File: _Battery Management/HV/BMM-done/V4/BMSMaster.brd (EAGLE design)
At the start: 88.9 x 79.7 mm, 120 parts, among them J1 M2_DF13-2P, J10 IMD, J2 M2_DF13-2P, J3 M4_1X4_LOCK, J4 M80022232081-2, J5 M16_M_194280016, J6 M2770166, J7 M2770166, J8 M2770166, J9 M2770166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

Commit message: BMM cleanup
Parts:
- added RE, RX, TX: TP, FSAE Electric:0603
- moved R6 3.30 mm to (70.5, 50.0), flipped to the bottom
- moved R9 2.80 mm to (68.0, 50.0), flipped to the bottom
- moved K1 2.29 mm to (8.64, 20.1)
- moved U23 2.04 mm to (6.76, 15.2)
- moved J9 1.65 mm to (20.2, 42.7)
- moved J7 0.89 mm to (27.1, 42.7)
- moved J10 0.76 mm to (26.3, 30.9)
- moved J8 0.64 mm to (40.8, 42.7)
- moved U$1 0.63 mm to (47.1, 46.3)
- moved R34 0.38 mm to (37.0, 32.4)
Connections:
- net RE: now also RE.1, RE.2
- net RX2: now also RX.1, RX.2
- net TX2: now also TX.1, TX.2
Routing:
- net VSS: track 103.3 -> 111.7 mm
- net +3V3: track 279.5 -> 271.7 mm, vias 68 -> 67
- net CS2: track 30.3 -> 34.9 mm
- net RX2: track 17.6 -> 22.0 mm
- net RE: track 30.0 -> 34.3 mm
- net TX2: track 21.0 -> 25.0 mm
- net +24V: track 117.0 -> 120.9 mm
- net N$22: track 6.49 -> 3.30 mm, vias 2 -> 1
- net N$3: track 6.37 -> 3.26 mm, vias 2 -> 1
- net BMS-SS: track 57.7 -> 59.8 mm
- net BMS-SET: track 65.9 -> 67.8 mm
- net PRE_CRG-B_AIR: track 23.1 -> 24.0 mm
- net INTERLOCK_IN: track 26.7 -> 26.0 mm
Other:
- outline, holes or cut-outs redrawn

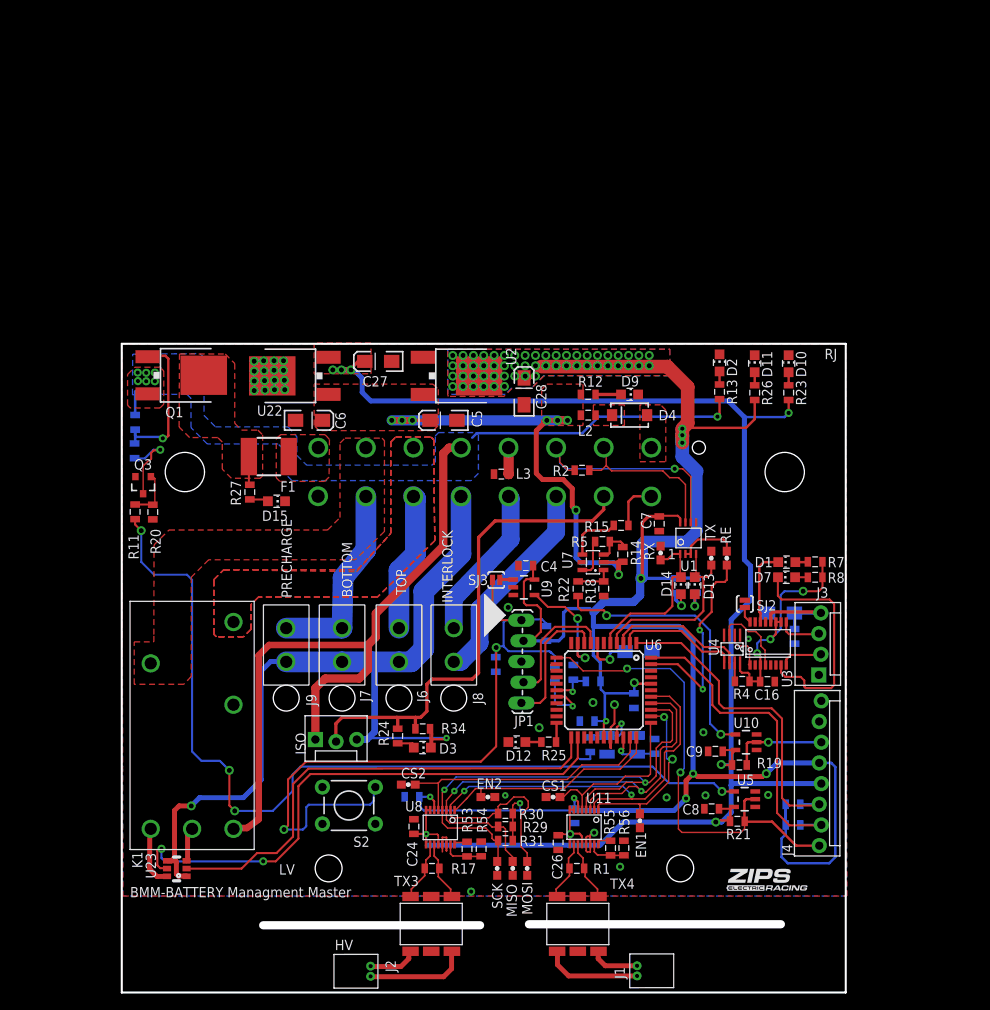
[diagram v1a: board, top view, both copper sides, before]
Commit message: Making board size change, make IO more accessible.
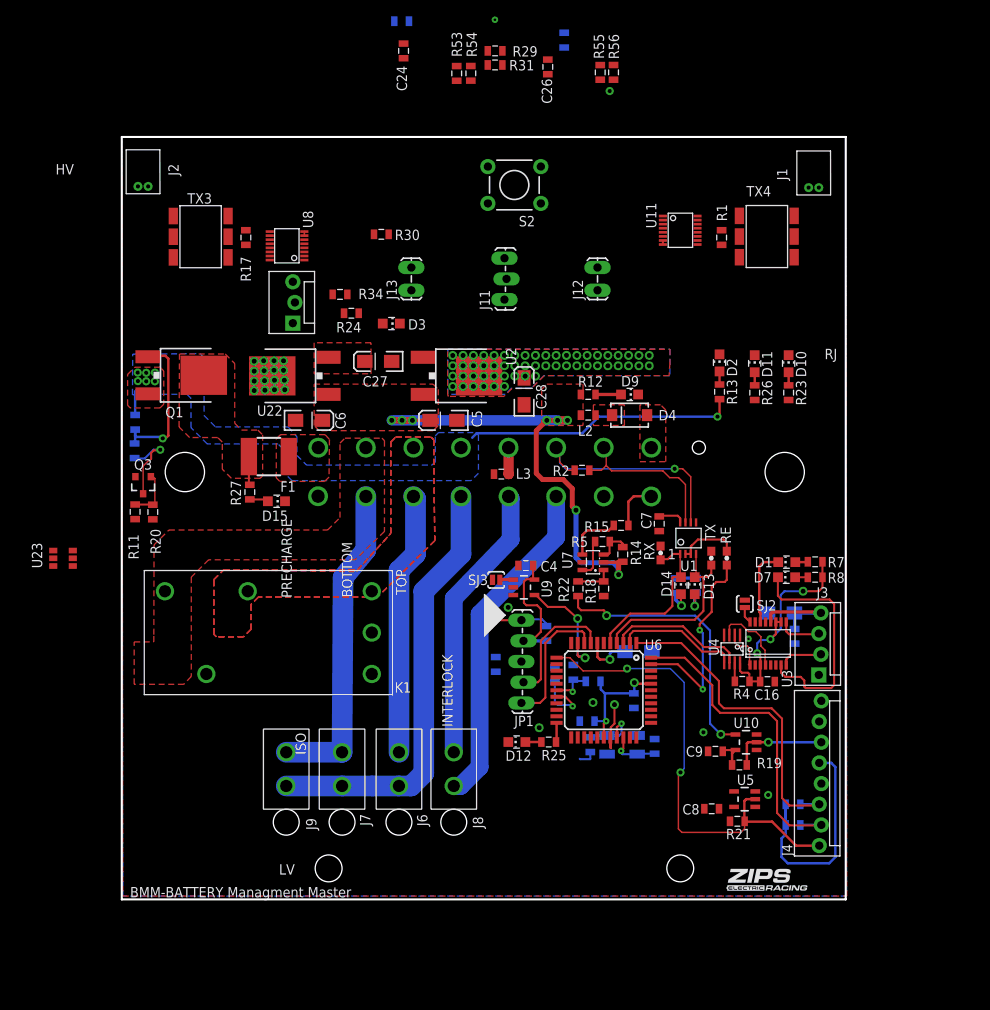
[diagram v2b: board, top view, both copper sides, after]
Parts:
- removed CS1, CS2, EN1, EN2, MISO, MOSI, SCK: TP, FSAE Electric:0603
- added J11: (no value), SparkFun-Connectors:1X03_LOCK_LONGPADS
- added J12, J13: (no value), SparkFun-Connectors:1X02_LOCK_LONGPADS
- moved J2 100.3 mm to (2.61, 99.0), turned to 0 degrees
- moved J1 98.6 mm to (85.0, 98.8), turned to 0 degrees
- moved C23 95.3 mm to (34.4, 119.3)
- moved C24 95.3 mm to (34.6, 115.6)
- moved C25 95.3 mm to (54.3, 117.0)
- moved C26 95.3 mm to (52.3, 113.7)
- moved R29 95.3 mm to (45.8, 115.6)
- moved R31 95.3 mm to (45.8, 113.9)
- moved R53 95.3 mm to (41.1, 112.9)
- moved R54 95.3 mm to (42.9, 112.9)
- moved R55 95.3 mm to (58.8, 113.0)
- moved R56 95.3 mm to (60.4, 113.0)
- moved TX3 89.0 mm to (9.68, 92.8), turned to 180 degrees
- moved TX4 87.6 mm to (79.2, 92.8), turned to 0 degrees
- moved R17 80.8 mm to (15.2, 92.7), turned to 90 degrees
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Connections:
- net CS1: now also J12.2; no longer CS1.1, CS1.2
- net CS2: now also J13.1; no longer CS2.1, CS2.2
- net EN1: now also J12.1; no longer EN1.1, EN1.2
- net EN2: now also J13.2; no longer EN2.1, EN2.2
- net MISO: now also J11.2; no longer MISO.1, MISO.2
- net MOSI: now also J11.3; no longer MOSI.1, MOSI.2
- net SCK: now also J11.1; no longer SCK.1, SCK.2
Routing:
- net +3V3: track 271.7 -> 67.8 mm, vias 67 -> 57
- net +5V: track 203.2 -> 4.64 mm, vias 8 -> 0
- net N$19: track 110.6 -> 0.00 mm, vias 4 -> 0
- net +24V: track 120.9 -> 36.8 mm
- net N$45: track 89.8 -> 6.32 mm, vias 2 -> 0
- net MOSI: track 71.7 -> 0.00 mm, vias 2 -> 0
- net BMS-SET: track 67.8 -> 0.00 mm, vias 2 -> 0
- net MISO: track 67.0 -> 0.00 mm, vias 2 -> 0
- net SCK: track 65.8 -> 0.00 mm, vias 2 -> 0
- net IMD: track 62.1 -> 0.00 mm
- net BMS-SS: track 59.8 -> 0.00 mm
- net VSS: track 111.7 -> 55.5 mm, vias 2 -> 0
- net CS2: track 34.9 -> 0.00 mm
- net EN2: track 30.0 -> 0.00 mm
- net EN1: track 23.9 -> 0.00 mm, vias 2 -> 0
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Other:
- board size 88.9 x 79.7 mm -> 88.9 x 93.6 mm

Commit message: playing w/ layout
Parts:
- moved R23 44.2 mm to (45.7, 99.1)
- moved D10 43.3 mm to (47.0, 102.9), turned to 270 degrees
- moved R26 37.0 mm to (50.8, 99.1)
- moved D11 36.3 mm to (52.1, 102.9), turned to 270 degrees
- moved R13 30.8 mm to (55.9, 99.1)
- moved D2 30.3 mm to (57.1, 102.9), turned to 270 degrees
- moved K1 28.4 mm to (2.32, 46.0), turned to 0 degrees
- moved S2 23.6 mm to (67.3, 85.2)
- moved J9 5.08 mm to (15.1, 27.4)
- moved J7 2.54 mm to (24.5, 27.4)
- moved U11 1.27 mm to (67.3, 93.6)
- moved J6 1.27 mm to (32.8, 27.4)
- moved R1 1.27 mm to (72.4, 92.7)
- moved TX4 1.27 mm to (78.0, 92.8)
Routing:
- net +24V: track 36.8 -> 3.34 mm, vias 7 -> 6
- net VSS: track 55.5 -> 67.7 mm
- net PRE_CRG-B_AIR: track 39.3 -> 42.8 mm
- net N$30: track 2.14 -> 0.00 mm
- net N$9: track 1.90 -> 0.00 mm
- net N$13: track 1.61 -> 0.00 mm
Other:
- board size 88.9 x 93.6 mm -> 88.9 x 94 mm

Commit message: Working on BMM
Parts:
- removed J4: M80022232081-2, FSAE Electric:MOLEX-1X8-2
- removed L5: L_FB_2A, FSAE Electric:0805
- removed STANDOFF3, STANDOFF4: STAND-OFF, SparkFun-Electromechanical:STAND-OFF
- removed U$2: LOGO16-2-M, Pic:2016-2-LOGO-M
- added C10: 0.1UF, FSAE Electric:0805
- added J14: USB_B_RA, FSAE Electric:USB-B1HSW6
- added U12: FT24C64A, FSAE Electric:SOT23-5
- J3: value M4_1X4_LOCK -> M8S08B-PASK-2(LF)(SN); device FSAE Electric:MOLEX_1X4 -> FSAE Electric:S08B-PASK-2(LF)(SN)
- S2: value (none) -> SWITCH-MOMENTARY-2SIDE_EZ; device SparkFun-Electromechanical:TACTILE-PTH -> SparkFun-Electromechanical:TACTILE-PTH-SIDEEZ
- moved D12 74.9 mm to (24.0, 101.5), turned to 0 degrees
- moved R25 72.1 mm to (25.8, 97.8), turned to 90 degrees
- moved C26 70.3 mm to (-11.6, 84.2)
- moved R7 69.3 mm to (34.4, 100.1), flipped to the bottom, turned to 270 degrees
- moved R8 69.1 mm to (36.5, 100.1), flipped to the bottom, turned to 270 degrees
- moved D1 67.2 mm to (34.2, 100.4), turned to 180 degrees
- moved D7 66.9 mm to (36.5, 100.4), turned to 180 degrees
- moved C20 64.6 mm to (41.5, 93.6), turned to 0 degrees
- moved C14 63.8 mm to (40.7, 96.1)
- moved C16 59.3 mm to (52.3, 91.0), flipped to the bottom, turned to 90 degrees
- moved C23 59.1 mm to (65.5, 69.0), turned to 270 degrees
- moved U22 58.3 mm to (76.5, 57.1), turned to 0 degrees
- moved U3 57.7 mm to (47.4, 90.9), turned to 90 degrees
- moved C6 55.6 mm to (74.5, 49.4)
- moved R4 54.7 mm to (51.3, 86.9), flipped to the bottom, turned to 90 degrees
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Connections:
- removed net N$21: C1.1, L5.2, U6.17
- net +3V3: now also C1.1, C10.1, J3.3, U12.4, U6.17; no longer J4.5, L5.1
- net +5V: now also J3.6; no longer J4.4
- net CS: now also J3.1; no longer J4.6
- net GND: now also C10.2, J14.4, J3.7, J3.8, U12.2, U12.5; no longer J3.1, J4.7, J4.8
- net HV-SENSE: now also J3.2; no longer J4.1
- net N$16: now also J14.2; no longer J3.3
- net N$18: now also J14.3; no longer J3.2
- net N$45: now also S2.2; no longer S2.3
- net N$85: now also J14.1; no longer J3.4
- net SCL: now also J3.5, U12.1; no longer J4.2
- net SDA: now also J3.4, U12.3; no longer J4.3
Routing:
- net MOSI: track 0.00 -> 97.4 mm, vias 0 -> 2
- net MISO: track 0.00 -> 92.1 mm, vias 0 -> 2
- net SCK: track 0.00 -> 88.1 mm, vias 0 -> 2
- net +9V: track 64.0 -> 0.00 mm, vias 8 -> 0
- net +3V3: track 67.8 -> 4.97 mm, vias 57 -> 0
- net CS2: track 0.00 -> 49.6 mm, vias 0 -> 1
- net HV-SENSE: track 59.3 -> 12.1 mm, vias 2 -> 0
- net +24V: track 3.34 -> 41.1 mm, vias 6 -> 0
- net N$48: track 16.6 -> 51.0 mm, vias 0 -> 1
- net N$41: track 34.1 -> 0.00 mm, vias 2 -> 0
- net N$47: track 15.5 -> 48.5 mm, vias 0 -> 1
- net 3V: track 28.9 -> 2.73 mm, vias 3 -> 0
- net VSS: track 67.7 -> 44.0 mm
- net TX2: track 25.0 -> 47.3 mm, vias 0 -> 2
- net RX2: track 22.0 -> 42.4 mm, vias 0 -> 2
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- added copper zone on layer 16, net N$31
- added copper zone on layer 16, net N$32
- removed copper zone on layer 1, net +24V
- removed copper zone on layer 16, net +24V
- removed copper zone on layer 1, net +3V3
- removed copper zone on layer 16, net +3V3
- removed copper zone on layer 1, net +5V
- removed copper zone on layer 1, net +9V
- removed copper zone on layer 1, net N$31
- removed copper zone on layer 1, net N$32
- removed copper zone on layer 1, net N$51
- removed copper zone on layer 1, net N$89
- removed copper zone on layer 1, net N$91
- removed copper zone on layer 1, net TSAL
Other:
- board size 88.9 x 94 mm -> 83.8 x 91.4 mm
